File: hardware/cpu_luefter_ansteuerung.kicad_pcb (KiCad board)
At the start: 2 copper layers, 50.8 x 67.3 mm, 28 parts, among them J1 Power 12V DC, J2 ISP, J3 CPU Lüfter, Q1 BC337, SW1 SW_Push, U1 7805, U2 ATtiny24A-PU, U3 74HC595, U4 KCSA02-123

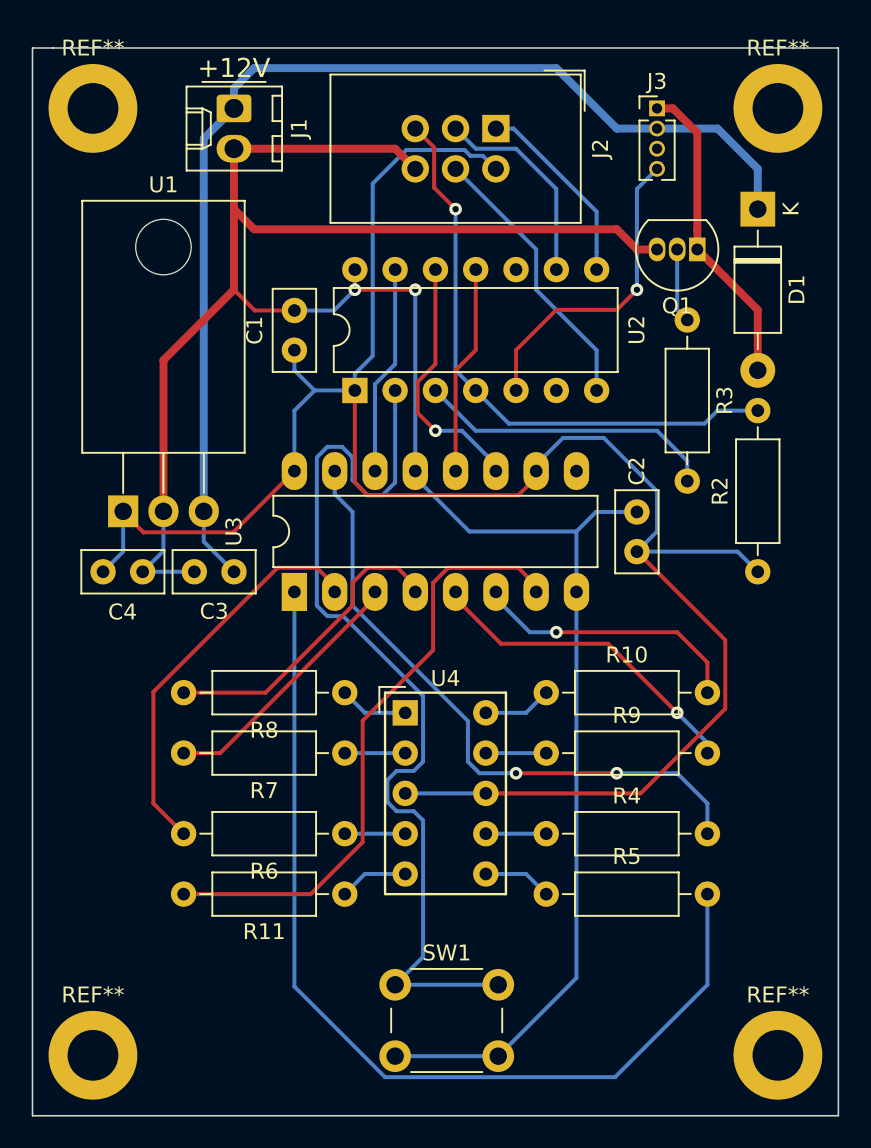
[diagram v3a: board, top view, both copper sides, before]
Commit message: Display + Taster auf Bottom Layer gelegt. STEP Datei erzeugt.
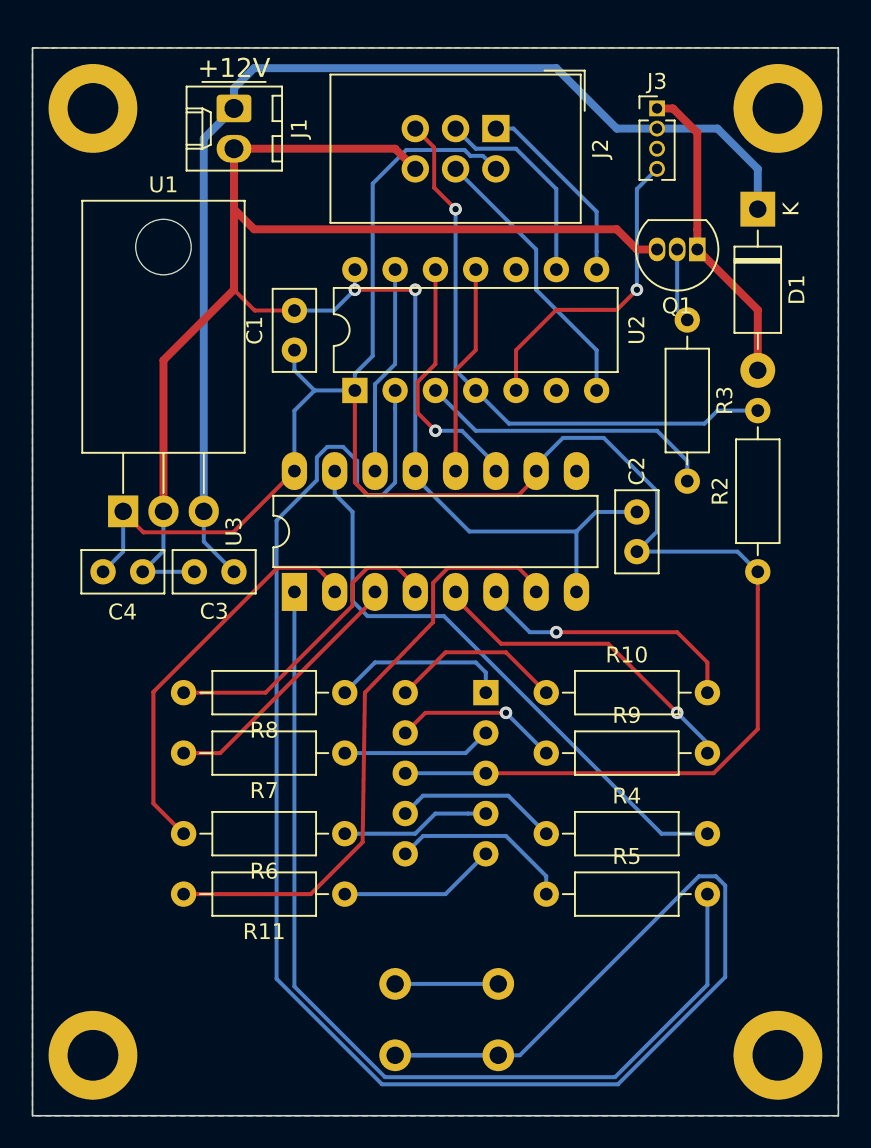
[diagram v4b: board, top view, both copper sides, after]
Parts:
- SW1, U4: moved to B.Cu
- moved U4 5.24 mm to (130.2, 113.0), turned to 180 degrees
- moved SW1 4.44 mm to (124.5, 135.9)
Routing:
- net PUSH_BUTTON1: track 60.4 -> 119.2 mm
- net GND: track 155.1 -> 123.8 mm
- net Net-(R5-Pad1): track 4.34 -> 11.5 mm
- net Net-(R8-Pad1): track 4.34 -> 11.2 mm
- net Net-(R10-Pad1): track 4.34 -> 11.0 mm
- net Net-(R9-Pad1): track 3.81 -> 10.5 mm, vias 0 -> 1
- net Net-(R4-Pad1): track 3.81 -> 10.3 mm
- net Net-(R7-Pad1): track 3.81 -> 9.42 mm
- net Net-(R11-Pad1): track 4.34 -> 9.94 mm
- net Net-(R6-Pad1): track 3.81 -> 9.42 mm
- net Net-(R4-Pad2): track 39.9 -> 37.1 mm, vias 2 -> 0
- net +5V: track 126.8 -> 125.5 mm
- added copper zone on B.Cu, net GND
- added copper zone on F.Cu, net GND

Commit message: PCB habe ich mit meinem Logo versehen und Beschriftet
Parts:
- added G***: LOGO, Kattanek Logo:logo_01_7_1mm_fsilk, F.Cu at (116.8, 134.0)
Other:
- board text added: "Lüftersteuerung Rev.: 2.4"
- board text added: "by Thorsten Kattanek"
- board text added: "https://github.com/ThKattanek/cpu_luefter_steuerung"

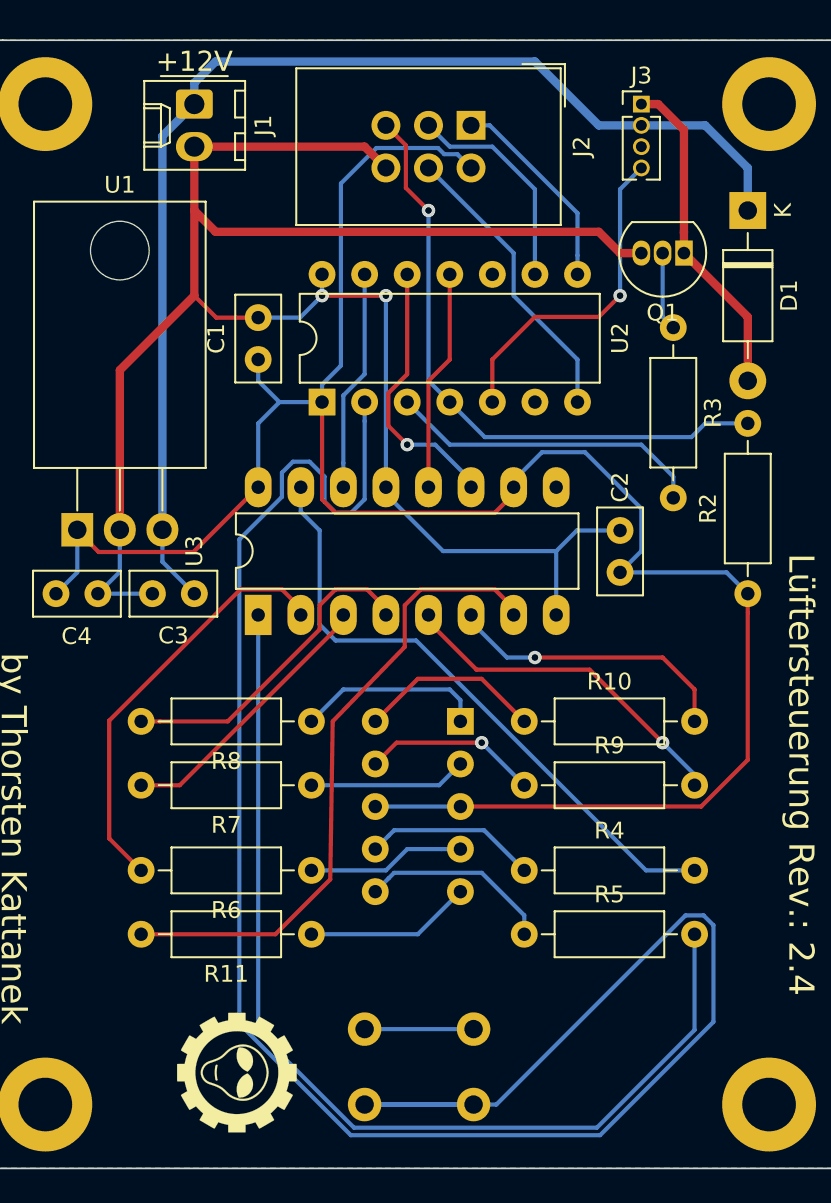
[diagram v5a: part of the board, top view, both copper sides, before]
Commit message: PCB - Bestückungsdruck bereinigt
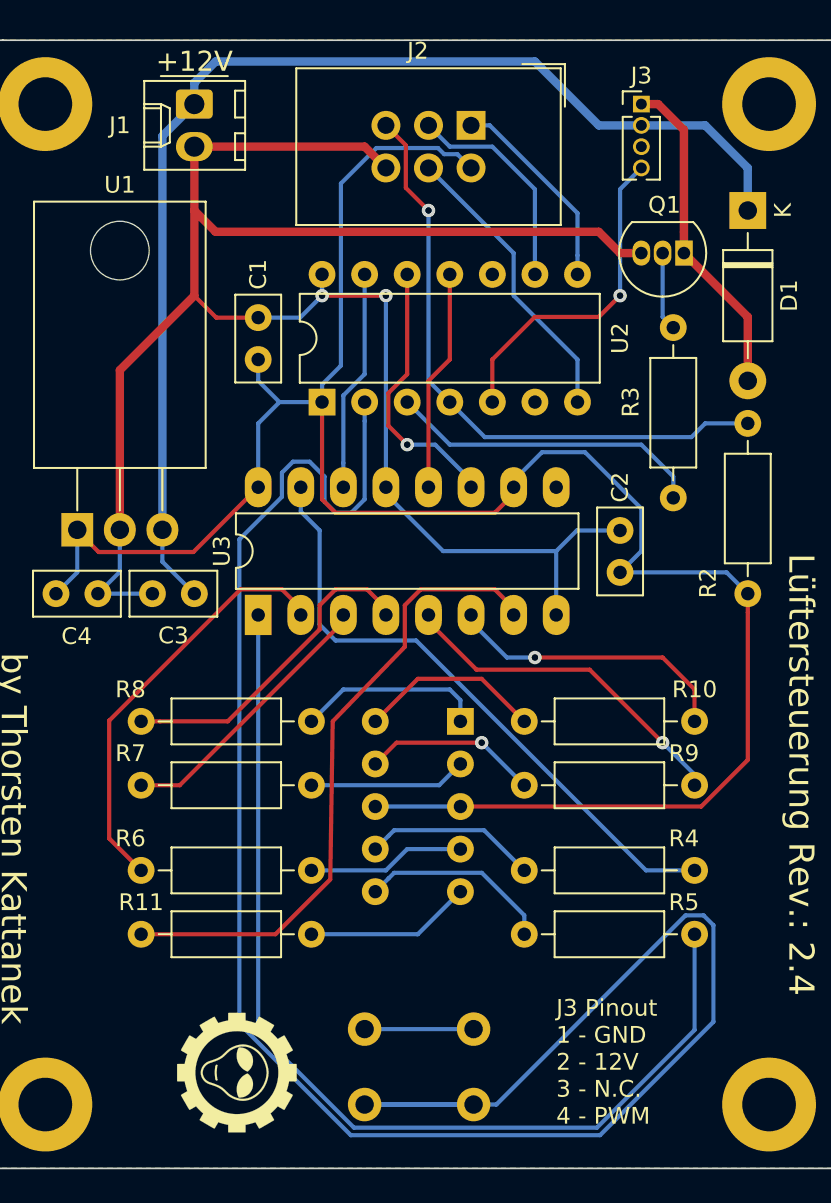
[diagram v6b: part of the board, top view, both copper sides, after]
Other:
- board text added: "J3 Pinout 1 - GND 2 - 12V 3 - N.C. 4 - PWM"
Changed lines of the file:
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@@
   (general
     (thickness 1.6)
-    (drawings 11)
+    (drawings 12)
     (tracks 237)
     (zones 0)
@@
     (47 F.CrtYd user)
     (48 B.Fab user)
-    (49 F.Fab user)
+    (49 F.Fab user hide)
   )
   (setup
@@
     (descr "C, Disc series, Radial, pin pitch=2.50mm, , diameter*width=5*2.5mm^2, Capacitor, http://cdn-reichelt.de/documents/datenblatt/B300/DS_KERKO_TC.pdf")
     (tags "C Disc series Radial pin pitch 2.50mm  diameter 5mm width 2.5mm Capacitor")
-    (fp_text reference C1 (at 1.25 -2.5 90) (layer F.SilkS)
+    (fp_text reference C1 (at 5.08 0 90) (layer F.SilkS)
       (effects (font (size 1 1) (thickness 0.15)))
     )
@@
     (descr "Molex KK-254 Interconnect System, old/engineering part number: AE-6410-02A example for new part number: 22-27-2021, 2 Pins (http://www.molex.com/pdm_docs/sd/022272021_sd.pdf), generated with kicad-footprint-generator")
     (tags "connector Molex KK-254 side entry")
-    (fp_text reference J1 (at 1.27 -4.12 90) (layer F.SilkS)
+    (fp_text reference J1 (at 1.27 4.445 180) (layer F.SilkS)
       (effects (font (size 1 1) (thickness 0.15)))
     )
@@
     (descr "Through hole straight IDC box header, 2x03, 2.54mm pitch, double rows")
     (tags "Through hole IDC box header THT 2x03 2.54mm double row")
-    (fp_text reference J2 (at 1.27 -6.604 90) (layer F.SilkS)
+    (fp_text reference J2 (at -4.445 3.175 180) (layer F.SilkS)
       (effects (font (size 1 1) (thickness 0.15)))
     )
@@
     (descr "TO-92 leads in-line, narrow, oval pads, drill 0.75mm (see NXP sot054_po.pdf)")
     (tags "to-92 sc-43 sc-43a sot54 PA33 transistor")
-    (fp_text reference Q1 (at 1.27 -3.56) (layer F.SilkS)
+    (fp_text reference Q1 (at 1.166823 2.8712) (layer F.SilkS)
       (effects (font (size 1 1) (thickness 0.15)))
     )
@@
     (descr "Resistor, Axial_DIN0207 series, Axial, Horizontal, pin pitch=10.16mm, 0.25W = 1/4W, length*diameter=6.3*2.5mm^2, http://cdn-reichelt.de/documents/datenblatt/B400/1_4W%23YAG.pdf")
     (tags "Resistor Axial_DIN0207 series Axial Horizontal pin pitch 10.16mm 0.25W = 1/4W length 6.3mm diameter 2.5mm")
-    (fp_text reference R2 (at 5.08 -2.37 90) (layer F.SilkS)
+    (fp_text reference R2 (at 0.635 -2.37 90) (layer F.SilkS)
       (effects (font (size 1 1) (thickness 0.15)))
     )
@@
     (descr "Resistor, Axial_DIN0207 series, Axial, Horizontal, pin pitch=10.16mm, 0.25W = 1/4W, length*diameter=6.3*2.5mm^2, http://cdn-reichelt.de/documents/datenblatt/B400/1_4W%23YAG.pdf")
     (tags "Resistor Axial_DIN0207 series Axial Horizontal pin pitch 10.16mm 0.25W = 1/4W length 6.3mm diameter 2.5mm")
-    (fp_text reference R3 (at 5.08 -2.37 90) (layer F.SilkS)
+    (fp_text reference R3 (at 4.445 2.54 90) (layer F.SilkS)
       (effects (font (size 1 1) (thickness 0.15)))
     )
@@
     (descr "Resistor, Axial_DIN0207 series, Axial, Horizontal, pin pitch=10.16mm, 0.25W = 1/4W, length*diameter=6.3*2.5mm^2, http://cdn-reichelt.de/documents/datenblatt/B400/1_4W%23YAG.pdf")
     (tags "Resistor Axial_DIN0207 series Axial Horizontal pin pitch 10.16mm 0.25W = 1/4W length 6.3mm diameter 2.5mm")
-    (fp_text reference R4 (at 5.08 -2.37) (layer F.SilkS)
+    (fp_text reference R4 (at 9.525 -1.905) (layer F.SilkS)
       (effects (font (size 1 1) (thickness 0.15)))
     )
@@
     (descr "Resistor, Axial_DIN0207 series, Axial, Horizontal, pin pitch=10.16mm, 0.25W = 1/4W, length*diameter=6.3*2.5mm^2, http://cdn-reichelt.de/documents/datenblatt/B400/1_4W%23YAG.pdf")
     (tags "Resistor Axial_DIN0207 series Axial Horizontal pin pitch 10.16mm 0.25W = 1/4W length 6.3mm diameter 2.5mm")
-    (fp_text reference R5 (at 5.08 -2.37) (layer F.SilkS)
+    (fp_text reference R5 (at 9.525 -1.905) (layer F.SilkS)
       (effects (font (size 1 1) (thickness 0.15)))
     )
@@
     (descr "Resistor, Axial_DIN0207 series, Axial, Horizontal, pin pitch=10.16mm, 0.25W = 1/4W, length*diameter=6.3*2.5mm^2, http://cdn-reichelt.de/documents/datenblatt/B400/1_4W%23YAG.pdf")
     (tags "Resistor Axial_DIN0207 series Axial Horizontal pin pitch 10.16mm 0.25W = 1/4W length 6.3mm diameter 2.5mm")
-    (fp_text reference R6 (at 5.08 -2.37) (layer F.SilkS)
+    (fp_text reference R6 (at 10.795 1.905) (layer F.SilkS)
       (effects (font (size 1 1) (thickness 0.15)))
     )
@@
     (descr "Resistor, Axial_DIN0207 series, Axial, Horizontal, pin pitch=10.16mm, 0.25W = 1/4W, length*diameter=6.3*2.5mm^2, http://cdn-reichelt.de/documents/datenblatt/B400/1_4W%23YAG.pdf")
     (tags "Resistor Axial_DIN0207 series Axial Horizontal pin pitch 10.16mm 0.25W = 1/4W length 6.3mm diameter 2.5mm")
-    (fp_text reference R7 (at 5.08 -2.37) (layer F.SilkS)
+    (fp_text reference R7 (at 10.795 1.905) (layer F.SilkS)
       (effects (font (size 1 1) (thickness 0.15)))
     )
@@
     (descr "Resistor, Axial_DIN0207 series, Axial, Horizontal, pin pitch=10.16mm, 0.25W = 1/4W, length*diameter=6.3*2.5mm^2, http://cdn-reichelt.de/documents/datenblatt/B400/1_4W%23YAG.pdf")
     (tags "Resistor Axial_DIN0207 series Axial Horizontal pin pitch 10.16mm 0.25W = 1/4W length 6.3mm diameter 2.5mm")
-    (fp_text reference R8 (at 5.08 -2.37) (layer F.SilkS)
+    (fp_text reference R8 (at 10.795 1.905) (layer F.SilkS)
       (effects (font (size 1 1) (thickness 0.15)))
     )
@@
     (descr "Resistor, Axial_DIN0207 series, Axial, Horizontal, pin pitch=10.16mm, 0.25W = 1/4W, length*diameter=6.3*2.5mm^2, http://cdn-reichelt.de/documents/datenblatt/B400/1_4W%23YAG.pdf")
     (tags "Resistor Axial_DIN0207 series Axial Horizontal pin pitch 10.16mm 0.25W = 1/4W length 6.3mm diameter 2.5mm")
-    (fp_text reference R9 (at 5.08 -2.37) (layer F.SilkS)
+    (fp_text reference R9 (at 9.525 -1.905) (layer F.SilkS)
       (effects (font (size 1 1) (thickness 0.15)))
     )
@@
     (descr "Resistor, Axial_DIN0207 series, Axial, Horizontal, pin pitch=10.16mm, 0.25W = 1/4W, length*diameter=6.3*2.5mm^2, http://cdn-reichelt.de/documents/datenblatt/B400/1_4W%23YAG.pdf")
     (tags "Resistor Axial_DIN0207 series Axial Horizontal pin pitch 10.16mm 0.25W = 1/4W length 6.3mm diameter 2.5mm")
-    (fp_text reference R10 (at 5.08 -2.37) (layer F.SilkS)
+    (fp_text reference R10 (at 10.16 -1.905) (layer F.SilkS)
       (effects (font (size 1 1) (thickness 0.15)))
     )
@@
     (descr "Resistor, Axial_DIN0207 series, Axial, Horizontal, pin pitch=10.16mm, 0.25W = 1/4W, length*diameter=6.3*2.5mm^2, http://cdn-reichelt.de/documents/datenblatt/B400/1_4W%23YAG.pdf")
     (tags "Resistor Axial_DIN0207 series Axial Horizontal pin pitch 10.16mm 0.25W = 1/4W length 6.3mm diameter 2.5mm")
-    (fp_text reference R11 (at 5.08 -2.37) (layer F.SilkS)
+    (fp_text reference R11 (at 10.16 1.905) (layer F.SilkS)
       (effects (font (size 1 1) (thickness 0.15)))
     )
@@
     (descr "16-lead though-hole mounted DIP package, row spacing 7.62 mm (300 mils), LongPads")
     (tags "THT DIP DIL PDIP 2.54mm 7.62mm 300mil LongPads")
-    (fp_text reference U3 (at 3.81 -3.81 90) (layer F.SilkS)
+    (fp_text reference U3 (at 3.81 -2.169135 90) (layer F.SilkS)
       (effects (font (size 1 1) (thickness 0.15)))
     )
@@
     )
   )
+  (gr_text "J3 Pinout\n1 - GND\n2 - 12V\n3 - N.C.\n4 - PWM" (at 135.89 133.35) (layer F.SilkS)
+    (effects (font (size 1 1) (thickness 0.15)) (justify left))
+  )
   (gr_text https://github.com/ThKattanek/cpu_luefter_steuerung (at 103.505 105.41 270) (layer B.SilkS)
